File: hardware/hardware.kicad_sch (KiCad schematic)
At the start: 0 parts

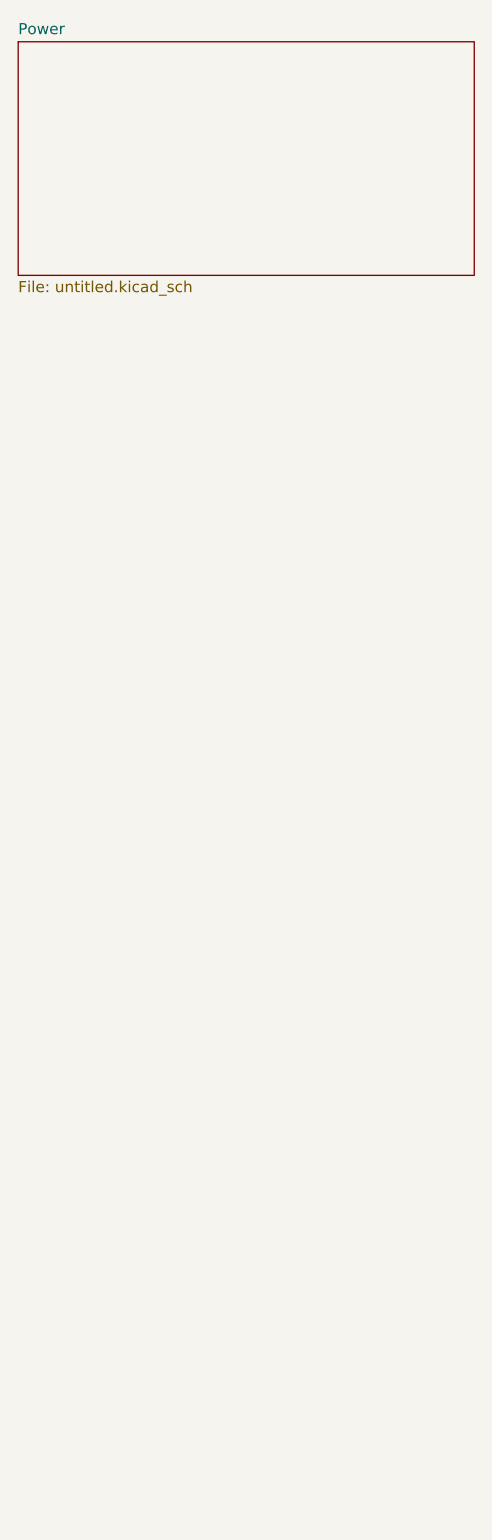
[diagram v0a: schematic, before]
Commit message: some power and ble additions to schematic
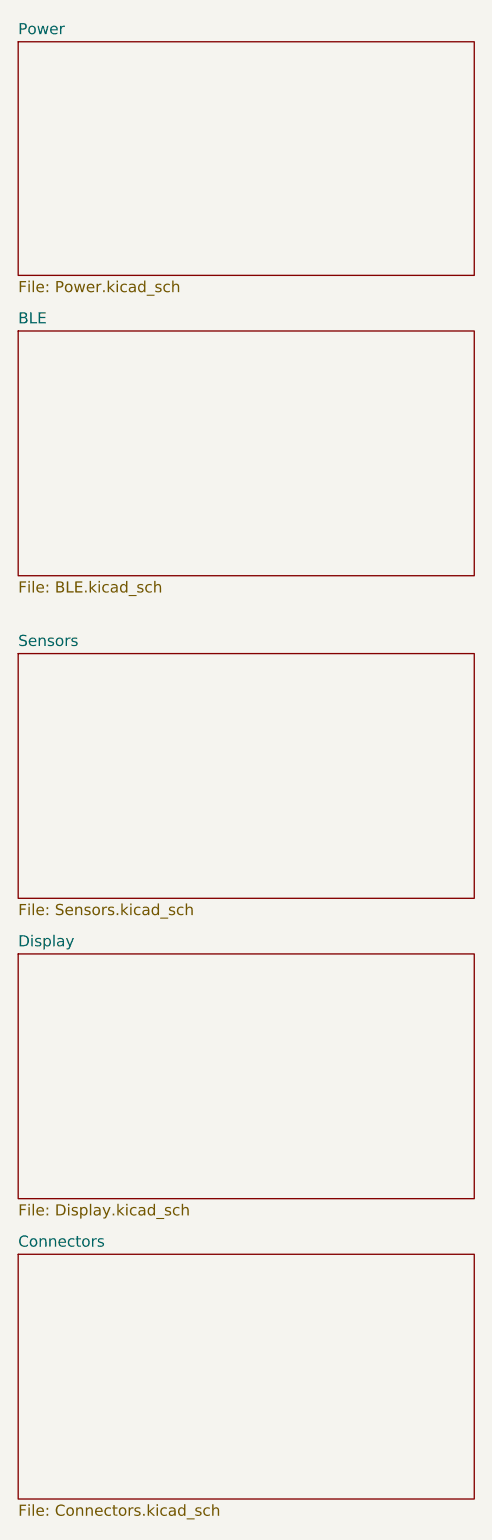
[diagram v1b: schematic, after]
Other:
- added sheet BLE (BLE.kicad_sch)
- added sheet Connectors (Connectors.kicad_sch)
- added sheet Display (Display.kicad_sch)
- added sheet Sensors (Sensors.kicad_sch)
- sheet Power: file untitled.kicad_sch -> Power.kicad_sch
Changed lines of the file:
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@@
     (rev "0.5")
+  )
+  (sheet (at 19.05 158.75) (size 52.07 27.94) (fields_autoplaced)
+    (stroke (width 0.1524) (type solid))
+    (fill (color 0 0 0 0.0000))
+    (property "Sheetname" "Connectors" (at 19.05 158.0384 0)
+      (effects (font (size 1.27 1.27)) (justify left bottom))
+    )
+    (property "Sheetfile" "Connectors.kicad_sch" (at 19.05 187.2746 0)
+      (effects (font (size 1.27 1.27)) (justify left top))
+    )
+    (property "Field2" "" (at 19.05 158.75 0)
+      (effects (font (size 1.27 1.27)) hide)
+    )
+    (instances
+      (project "hardware"
+        (path "/37151b3b-08b1-42f0-b823-5b7041c54301" (page "6"))
+      )
+    )
   )
   (sheet (at 19.05 20.32) (size 52.07 26.67) (fields_autoplaced)
@@
       (effects (font (size 1.27 1.27)) (justify left bottom))
     )
-    (property "Sheetfile" "untitled.kicad_sch" (at 19.05 47.5746 0)
+    (property "Sheetfile" "Power.kicad_sch" (at 19.05 47.5746 0)
       (effects (font (size 1.27 1.27)) (justify left top))
     )
@@
       )
     )
+  )
+  (sheet (at 19.05 90.17) (size 52.07 27.94) (fields_autoplaced)
+    (stroke (width 0.1524) (type solid))
+    (fill (color 0 0 0 0.0000))
+    (property "Sheetname" "Sensors" (at 19.05 89.4584 0)
+      (effects (font (size 1.27 1.27)) (justify left bottom))
+    )
+    (property "Sheetfile" "Sensors.kicad_sch" (at 19.05 118.6946 0)
+      (effects (font (size 1.27 1.27)) (justify left top))
+    )
+    (instances
+      (project "hardware"
+        (path "/37151b3b-08b1-42f0-b823-5b7041c54301" (page "4"))
+      )
+    )
+  )
+  (sheet (at 19.05 124.46) (size 52.07 27.94) (fields_autoplaced)
+    (stroke (width 0.1524) (type solid))
+    (fill (color 0 0 0 0.0000))
+    (property "Sheetname" "Display" (at 19.05 123.7484 0)
+      (effects (font (size 1.27 1.27)) (justify left bottom))
+    )
+    (property "Sheetfile" "Display.kicad_sch" (at 19.05 152.9846 0)
+      (effects (font (size 1.27 1.27)) (justify left top))
+    )
+    (instances
+      (project "hardware"
+        (path "/37151b3b-08b1-42f0-b823-5b7041c54301" (page "5"))
+      )
+    )
+  )
+  (sheet (at 19.05 53.34) (size 52.07 27.94) (fields_autoplaced)
+    (stroke (width 0.1524) (type solid))
+    (fill (color 0 0 0 0.0000))
+    (property "Sheetname" "BLE" (at 19.05 52.6284 0)
+      (effects (font (size 1.27 1.27)) (justify left bottom))
+    )
+    (property "Sheetfile" "BLE.kicad_sch" (at 19.05 81.8646 0)
+      (effects (font (size 1.27 1.27)) (justify left top))
+    )
+    (instances
+      (project "hardware"
+        (path "/37151b3b-08b1-42f0-b823-5b7041c54301" (page "3"))
+      )
+    )
